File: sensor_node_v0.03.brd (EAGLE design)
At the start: 46.8 x 39.9 mm, 50 parts, among them IC1 MCP1703CB, IC2 MCP1703CB, Q1 MMBT5088-NPN, U1 ATMEGA328P_TQFP, U2 TSL2561FN, U4 MPL115A, Y1 16MHZ

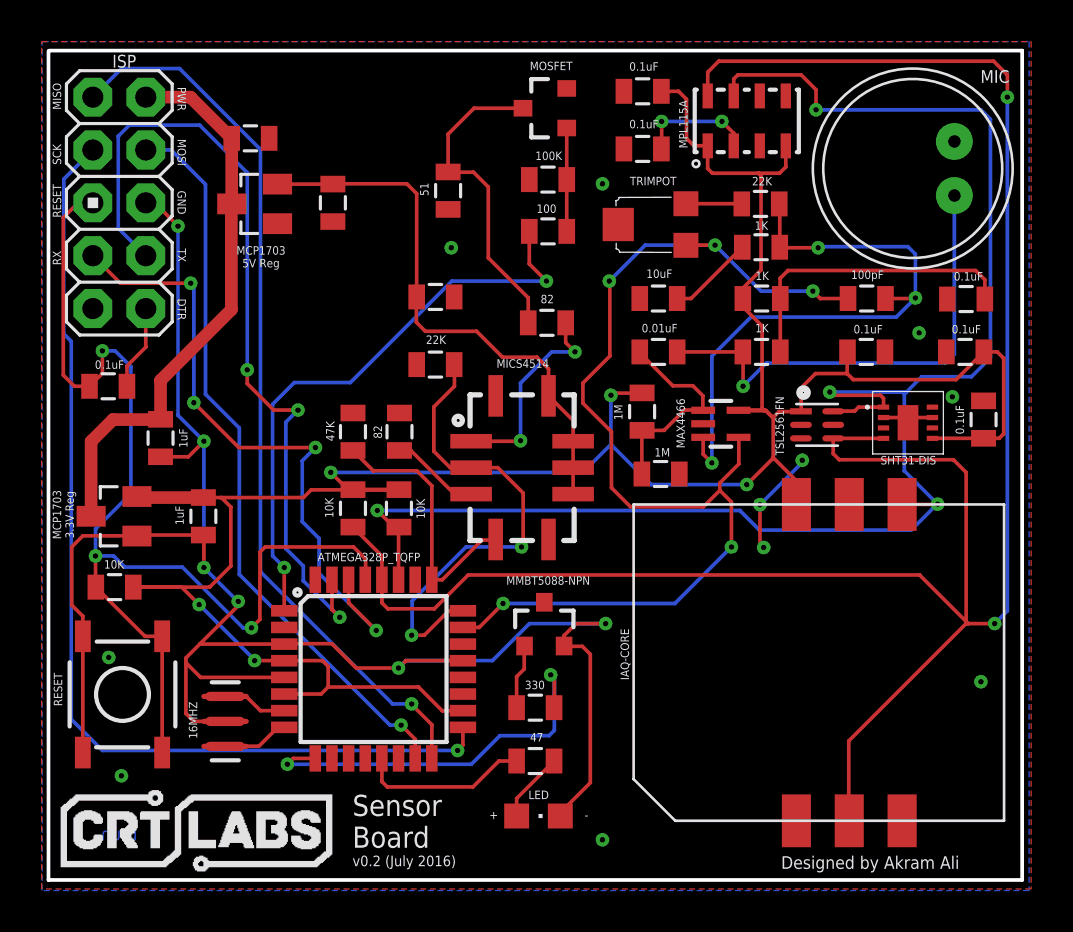
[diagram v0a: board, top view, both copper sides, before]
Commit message: Replaced mic
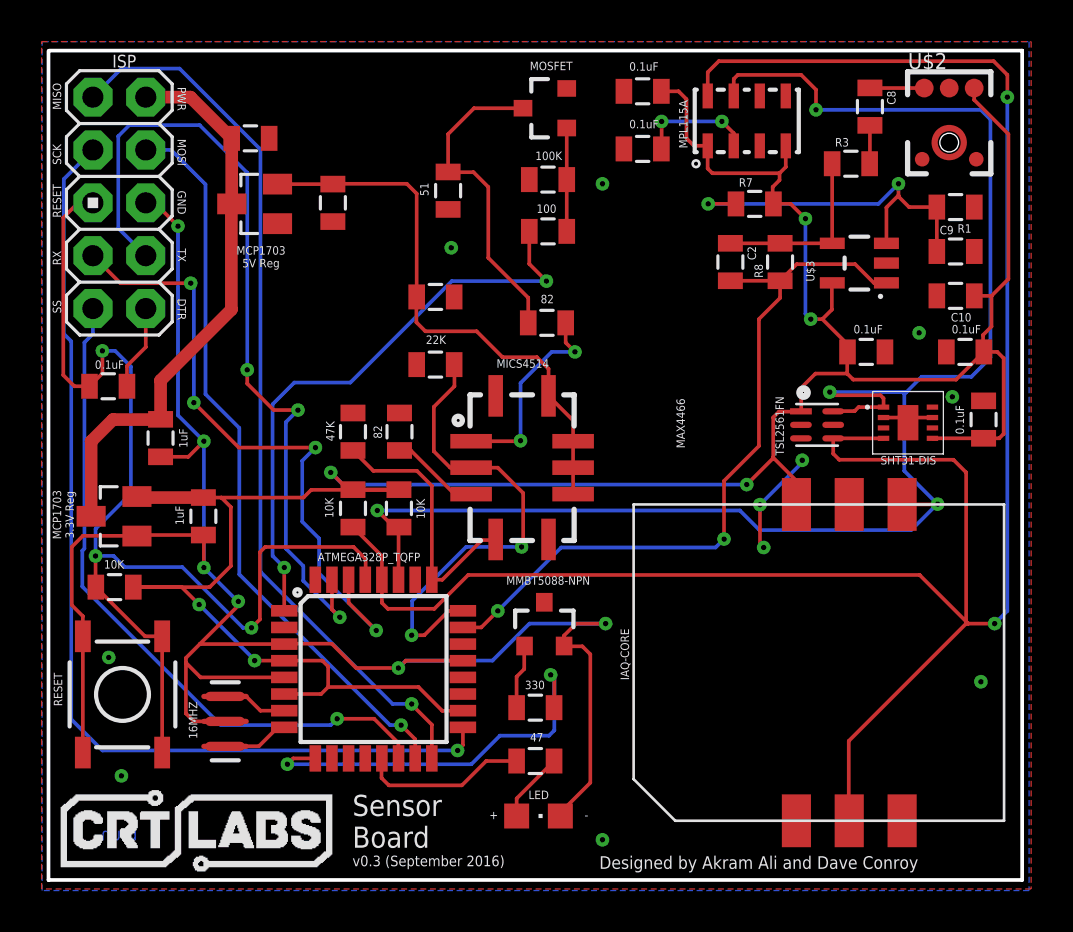
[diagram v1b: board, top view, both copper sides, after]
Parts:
- removed C11: 100pF, SparkFun-Passives:0805
- removed MIC: (no value), microbuilder:ELECTRET_9.7
- removed R10, R11, R9: 1K, SparkFun-Passives:0805
- removed R12: 22K, SparkFun-Passives:0805
- removed TRIMPOT: (no value), microbuilder:TRIMPOT_BOURNS_TC33X-2
- removed U3: (no value), microbuilder:SC70-5
- added C2: 100pF, SparkFun-Capacitors:0805
- added R1: 10K, SparkFun-Passives:0805
- added R3: 1.5K, SparkFun-Passives:0805
- added U$2: ADMP401, SparkFun-Sensors:ADMP401
- added U$3: OPA344, SparkFun-AnalogIC:SOT23-5
- C10: value 10uF -> 0.1uF; device SparkFun-Passives:0805 -> SparkFun-Capacitors:0805
- C8: value 0.01uF -> 4.7uF; device SparkFun-Passives:0805 -> SparkFun-Capacitors:0805
- C9: value 0.1uF -> 1uF; device SparkFun-Passives:0805 -> SparkFun-Capacitors:0805
- R7: value 1M -> 10K
- R8: value 1M -> 100K
- moved C8 15.6 mm to (45.4, 43.8), turned to 270 degrees
- moved C10 14.3 mm to (49.5, 34.7)
- moved R8 11.7 mm to (41.0, 36.3), turned to 90 degrees
- moved R7 11.4 mm to (39.8, 39.1), turned to 0 degrees
- moved C9 2.34 mm to (49.5, 36.8), turned to 0 degrees
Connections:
- removed net N$15: C10.1, R11.1
- removed net N$16: R12.2, TRIMPOT.3
- removed net N$6: C8.2, R7.1, R8.2, U3.1
- new net N$11: C9.1, R1.2, R7.1, U$3.3
- new net SS: J2.9, U1.14
- net A0: now also C2.2, R8.1, U$3.1; no longer C11.2, TRIMPOT.1, U3.4
- net GND0: now also R1.1, U$2.2, U$2.4, U$2.6, U$3.2; no longer MIC.-, R8.1, U3.2
- net N$10: now also C2.1, R3.1, R8.2, U$3.4; no longer C9.1, R10.1, R9.2
- net N$7: now also C8.1, U$2.1; no longer C11.1, R11.2, R12.1, U3.3
- net N$9: now also C8.2, R3.2; no longer C8.1, MIC.+, R9.1
- net VCC: now also C10.1, U$2.5, U$3.5; no longer R10.2, U3.5
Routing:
- net SS: track 0.00 -> 32.9 mm, vias 0 -> 1
- net N$7: track 29.8 -> 2.61 mm, vias 3 -> 0
- net N$9: track 23.2 -> 1.85 mm, vias 1 -> 0
- net N$11: track 0.00 -> 18.2 mm, vias 0 -> 2
- net A0: track 52.0 -> 36.1 mm, vias 5 -> 2
- net N$6: track 10.1 -> 0.00 mm
- net VCC: track 125.8 -> 132.6 mm, vias 5 -> 6
- net N$10: track 14.9 -> 8.73 mm
- net N$15: track 4.15 -> 0.00 mm
- net N$16: track 2.69 -> 0.00 mm
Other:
- board text added: "Designed by Akram Ali and Dave Conroy"
- board text added: "SS"
- board text added: "v0.3 (September 2016)"
- board text removed: "Designed by Akram Ali"
- board text removed: "v0.2 (July 2016)"

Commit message: Added RFM69 pads, FTDI chip, USB-microB, bug fixes
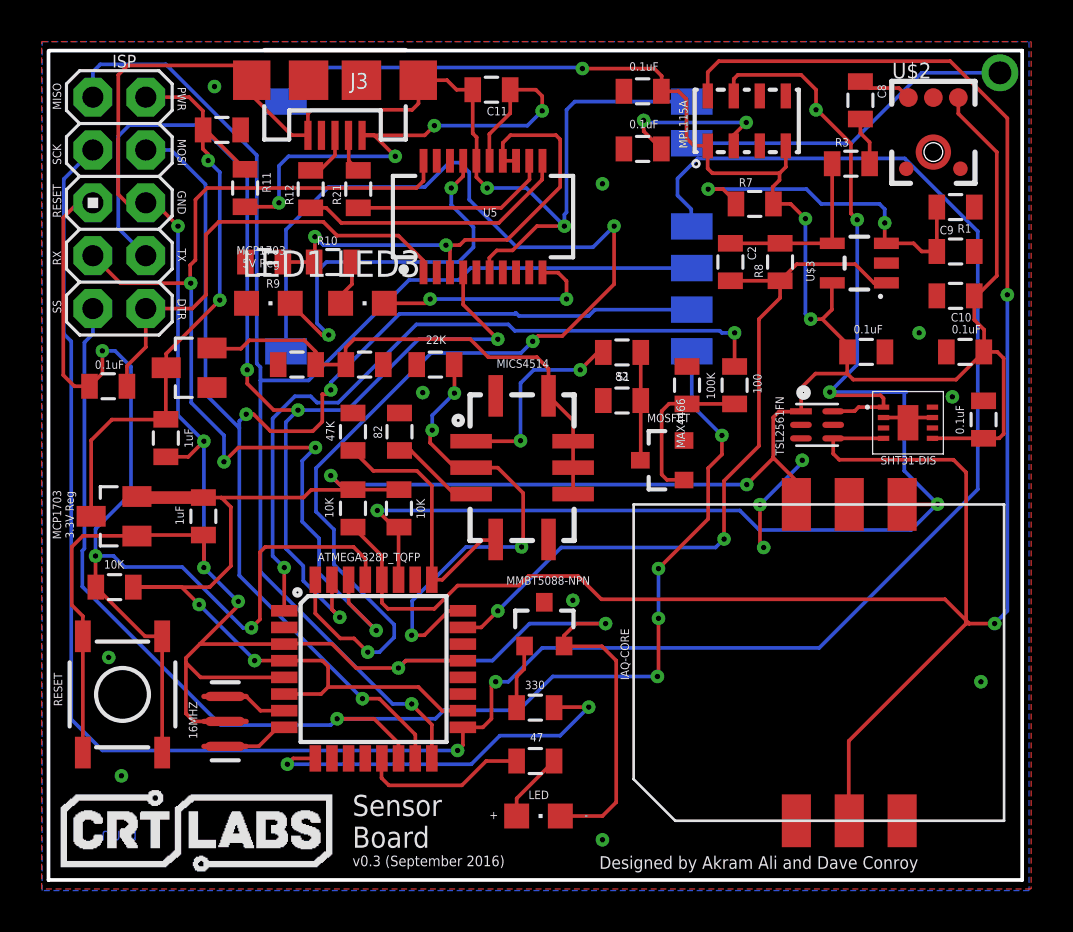
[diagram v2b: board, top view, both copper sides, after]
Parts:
- added C11: 0.1uF, SparkFun-Capacitors:0805
- added J3: USB-MICROB, SparkFun-Connectors:USB-MICROB
- added LED1, LED3: (no value), adafruit:CHIPLED_0805
- added R10, R9: 47, SparkFun-Passives:0805
- added R11: SHOTTKY, SparkFun-Passives:0805
- added R12, R21: 27, SparkFun-Passives:0805
- added U$4: LOWPOWERLAB_RFM69, RFM69 USB Gateway:LOWPOWERLAB_RFM69W-MINPADS
- added U5: FT231XS, SparkFun-DigitalIC:SSOP20_L
- moved MOSFET 17.8 mm to (35.4, 26.8)
- moved R17 13.1 mm to (33.5, 29.7), turned to 0 degrees
- moved R19 11.9 mm to (36.6, 30.4), turned to 270 degrees
- moved R20 11.6 mm to (38.9, 30.4), turned to 90 degrees
- moved IC2 8.48 mm to (12.6, 31.2)
- moved C17 7.96 mm to (17.8, 31.4), turned to 180 degrees
- moved C7 4.71 mm to (21.1, 31.4)
- moved R18 3.88 mm to (33.5, 32.0), turned to 180 degrees
- moved C16 1.43 mm to (14.2, 42.7)
- moved U$2 0.89 mm to (48.4, 41.6)
- moved C8 0.55 mm to (44.9, 44.1)
- moved C1 0.25 mm to (11.5, 27.9)
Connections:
- new net ANT: U$4.ANA
- new net D2: U$4.DIO0, U1.32
- new net FTDI_VCC: R10.1, R9.1, U5.13, U5.14, U5.3
- new net N$17: LED1.C, U5.17
- new net N$18: LED3.C, U5.10
- new net N$24: C11.1, J3.VBUS, R11.2, U5.15
- new net N$25: R21.1, U5.12
- new net N$26: R12.1, U5.11
- new net N$27: LED1.A, R9.2
- new net N$29: LED3.A, R10.2
- new net N$32: J3.D-, R21.2
- new net N$33: J3.D+, R12.2
- net DTR: now also U5.1
- net GND: now also C11.2, J3.GND, J3.MT1, J3.MT2, U$4.GND, U5.16, U5.6
- net MISO: now also U$4.MISO
- net MOSI: now also U$4.MOSI
- net PWR: now also R11.1
- net RX: now also U5.20
- net SCK: now also U$4.SCK
- net SS: now also U$4.NSS
- net TX: now also U5.4
- net VCC: now also U$4.VDD
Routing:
- net D2: track 0.00 -> 62.8 mm, vias 0 -> 3
- net SCK: track 48.5 -> 110.1 mm, vias 1 -> 2
- net GND: track 92.9 -> 150.7 mm, vias 6 -> 8
- net SS: track 32.9 -> 66.6 mm, vias 1 -> 5
- net N$24: track 0.00 -> 26.6 mm, vias 0 -> 4
- net MOSI: track 35.6 -> 61.9 mm, vias 1 -> 3
- net FTDI_VCC: track 0.00 -> 25.0 mm, vias 0 -> 2
- net MISO: track 43.5 -> 67.1 mm
- net N$17: track 0.00 -> 18.6 mm, vias 0 -> 2
- net DTR: track 4.11 -> 22.3 mm
- net RX: track 31.3 -> 49.3 mm
- net VCC: track 132.6 -> 149.2 mm, vias 6 -> 7
- net ANT: track 0.00 -> 16.2 mm, vias 0 -> 1
- net TX: track 40.0 -> 54.9 mm, vias 3 -> 4
- net N$26: track 0.00 -> 13.2 mm
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
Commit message: GND0 plane fix
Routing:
- net GND0: vias 13 -> 14
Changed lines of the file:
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@@
 <via x="13.8684" y="44.7548" extent="1-16" drill="0.254" diameter="0.127"/>
 <via x="31.0896" y="20.066" extent="1-16" drill="0.254" diameter="0.127"/>
-<wire x1="16.9308" y1="31.3944" x2="15.124" y2="42.672" width="0" layer="19" extent="1-1"/>
+<via x="30.5308" y="44.7548" extent="1-16" drill="0.254" diameter="0.127"/>
 </signal>
 <signal name="D5">

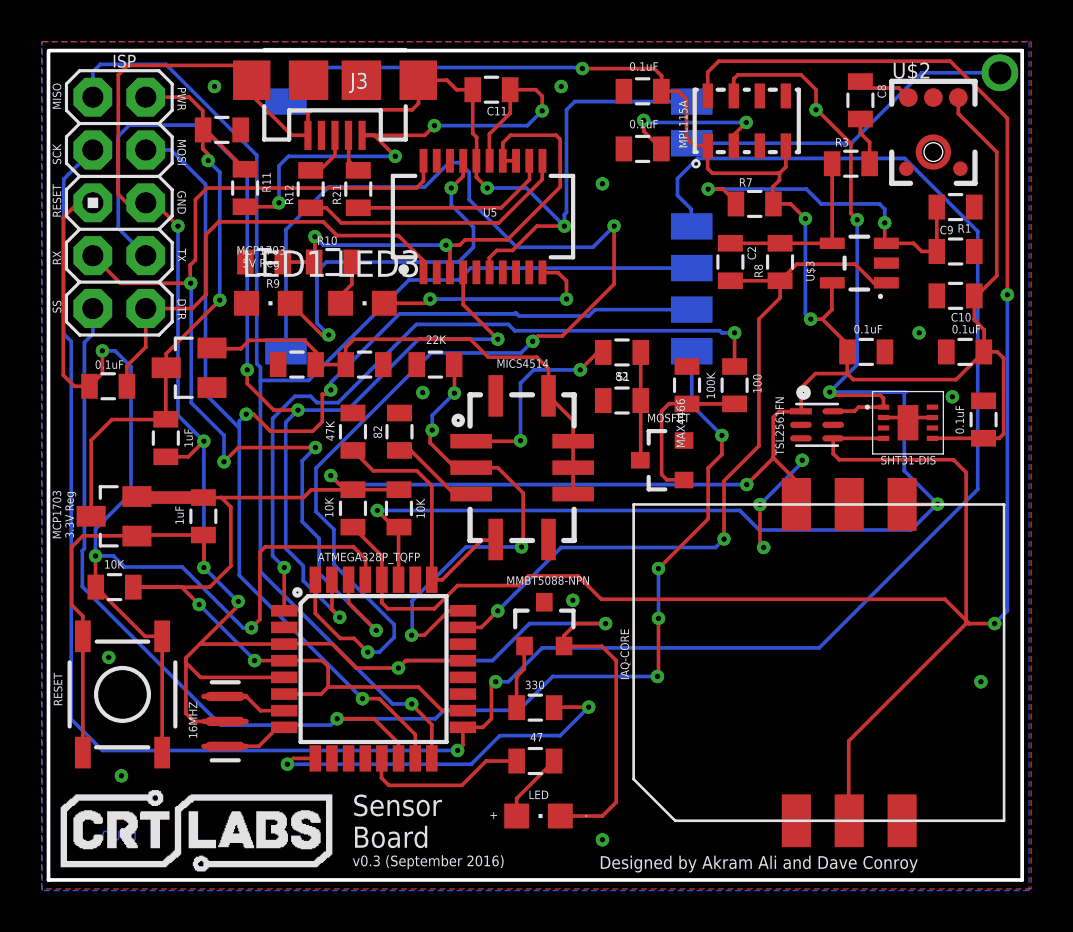
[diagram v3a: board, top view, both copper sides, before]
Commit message: Changed font size of labels
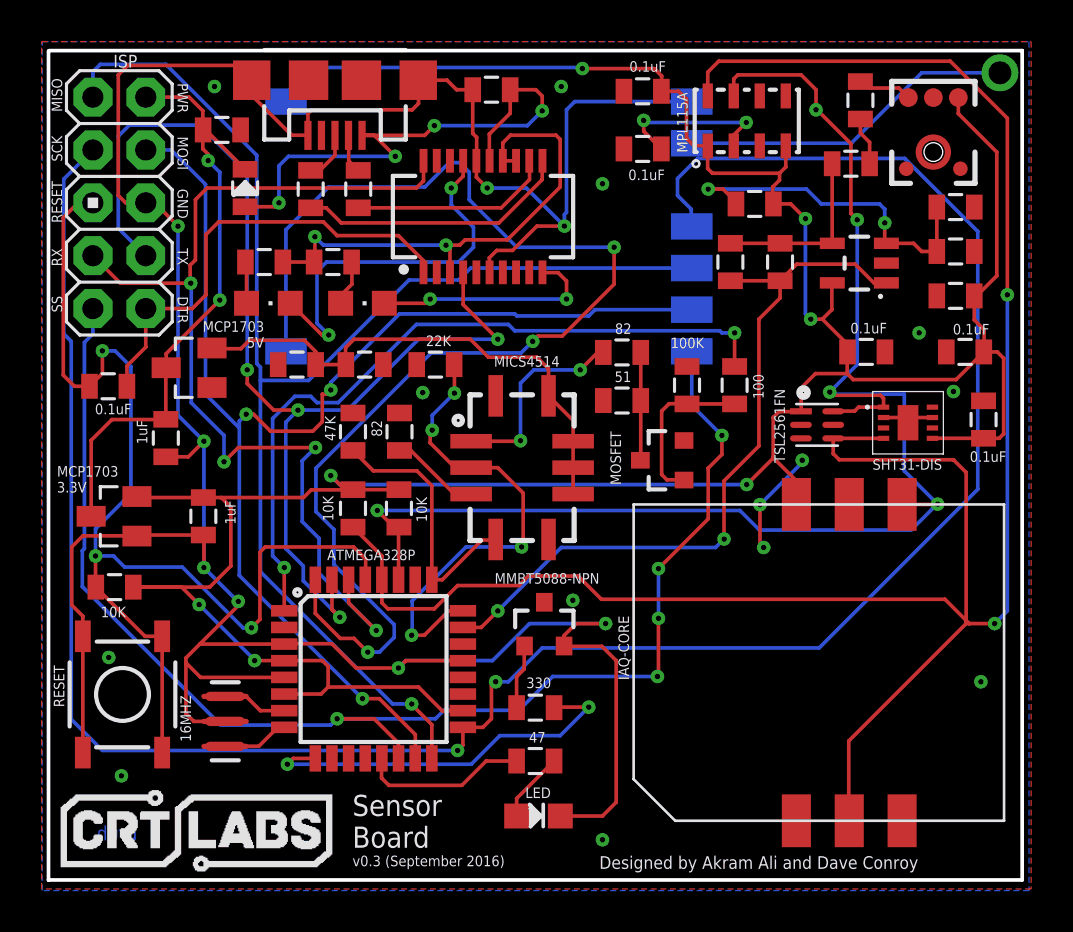
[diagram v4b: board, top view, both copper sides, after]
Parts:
- U$4: value LOWPOWERLAB_RFM69 -> RFM69HW
- U1: value ATMEGA328P_TQFP -> ATMEGA328P
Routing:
- net N$27: track 0.00 -> 2.00 mm
- net D2: track 62.8 -> 61.3 mm
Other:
- board text added: "MCP1703 3.3V"
- board text added: "MCP1703 5V"
- board text removed: "+"
- board text removed: "-"
- board text removed: "MAX4466"
- board text removed: "MCP1703 3.3V Reg"
- board text removed: "MCP1703 5V Reg"
